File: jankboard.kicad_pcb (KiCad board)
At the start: 2 copper layers, 152.4 x 85.7 mm, 154 parts, among them J1 F31L-1A7H1-11030, J2 F31L-1A7H1-11030, J3 Conn_01x02, J4 Conn_01x02, SW1 SW_Push_45deg, SW10 SW_Push_45deg, SW11 SW_Push_45deg, SW12 SW_Push_45deg, SW13 SW_Push_45deg, SW14 SW_Push_45deg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

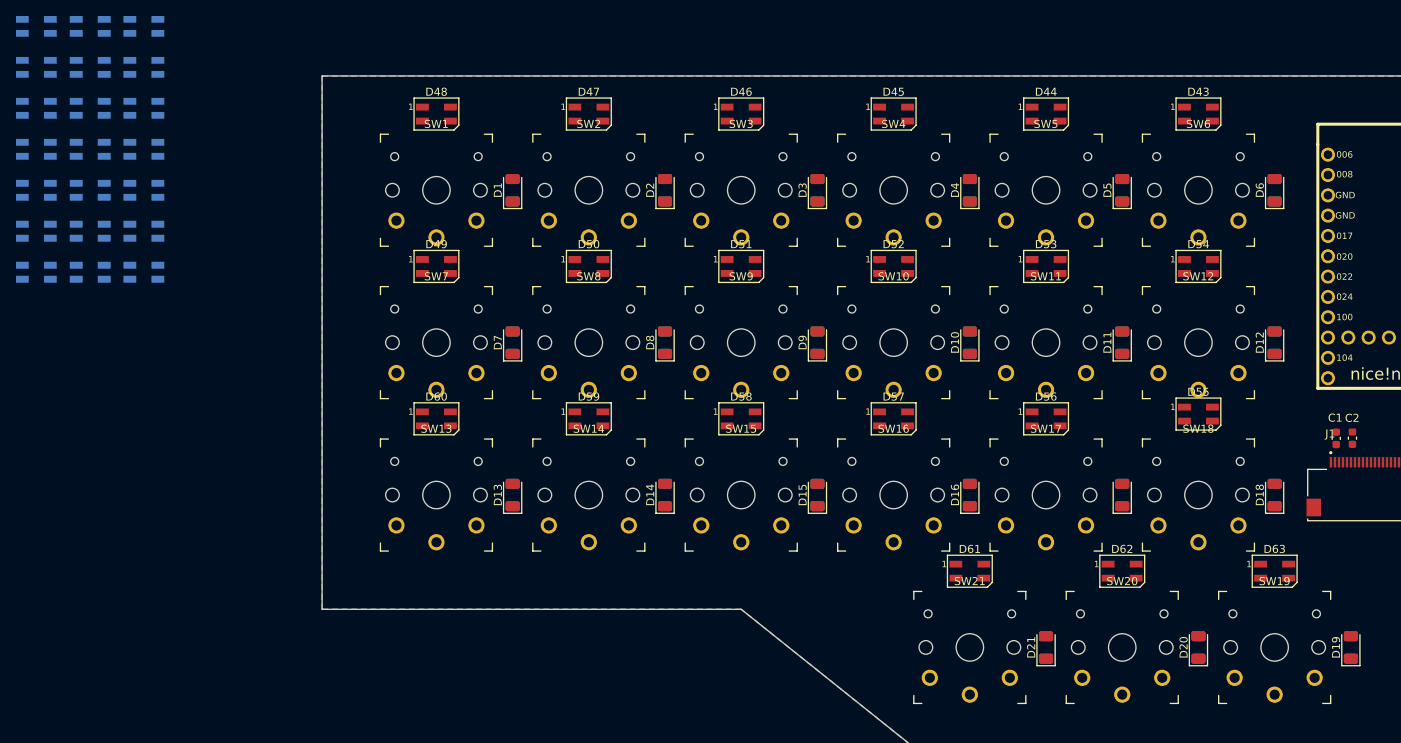
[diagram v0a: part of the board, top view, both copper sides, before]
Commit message: wired up matrix
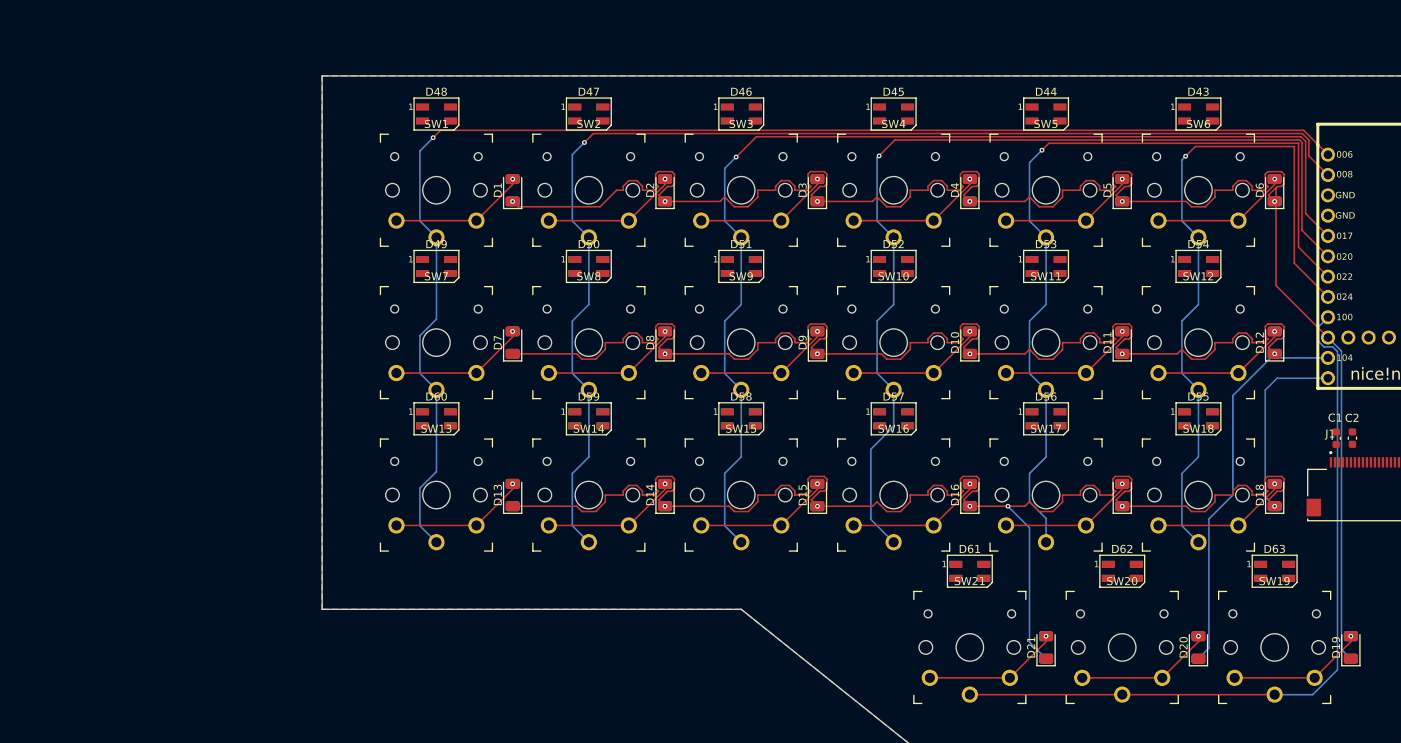
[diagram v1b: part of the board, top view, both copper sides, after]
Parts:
- moved D84 159.2 mm to (142.9, 85.7)
- moved D83 142.2 mm to (123.8, 85.7)
- moved D76 140.5 mm to (133.3, 66.7), turned to 0 degrees
- moved D75 138.9 mm to (133.3, 47.6)
- moved D64 132.3 mm to (133.3, 28.6), turned to 0 degrees
- moved D82 126.0 mm to (104.8, 85.7)
- moved D77 120.9 mm to (114.3, 66.7), turned to 0 degrees
- moved D74 120.4 mm to (114.3, 47.6)
- moved D78 117.9 mm to (95.2, 66.7), turned to 0 degrees
- moved D65 112.9 mm to (114.3, 28.6), turned to 0 degrees
- moved D73 102.4 mm to (95.2, 47.6)
- moved D79 98.5 mm to (76.2, 66.7), turned to 0 degrees
- moved D66 93.7 mm to (95.2, 28.6), turned to 0 degrees
- moved D72 85.1 mm to (76.2, 47.6)
- moved D80 79.2 mm to (57.1, 66.7), turned to 0 degrees
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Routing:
- net ROW0: track 0.00 -> 218.1 mm, vias 0 -> 6
- net ROW1: track 0.00 -> 204.2 mm, vias 0 -> 5
- net ROW2: track 0.00 -> 199.8 mm, vias 0 -> 6
- net COL0: track 0.00 -> 169.0 mm, vias 0 -> 1
- net COL1: track 0.00 -> 151.6 mm, vias 0 -> 1
- net COL2: track 0.00 -> 138.5 mm, vias 0 -> 1
- net COL3: track 0.00 -> 122.7 mm, vias 0 -> 1
- net COL4: track 0.00 -> 104.5 mm, vias 0 -> 1
- net COL6: track 0.00 -> 93.4 mm
- net COL5: track 0.00 -> 87.4 mm, vias 0 -> 1
- net Net-(D19-A): track 0.00 -> 17.1 mm, vias 0 -> 1
- net Net-(D18-A): track 0.00 -> 17.1 mm, vias 0 -> 1
- net Net-(D17-A): track 0.00 -> 17.1 mm, vias 0 -> 1
- net Net-(D16-A): track 0.00 -> 17.1 mm, vias 0 -> 1
- net Net-(D12-A): track 0.00 -> 17.1 mm, vias 0 -> 1
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
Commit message: neopixels
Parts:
- turned D49 to 180 degrees
- turned D50 to 180 degrees
- turned D51 to 180 degrees
- turned D52 to 180 degrees
- turned D53 to 180 degrees
- turned D54 to 180 degrees
- turned D61 to 180 degrees
- turned D62 to 180 degrees
- turned D63 to 180 degrees
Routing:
- net +3.3V: track 0.00 -> 535.6 mm, vias 0 -> 22
- net Net-(D60-DOUT): track 0.00 -> 90.0 mm
- net Net-(D81-DOUT): track 0.00 -> 85.3 mm, vias 0 -> 2
- net Net-(D75-DOUT): track 0.00 -> 24.1 mm, vias 0 -> 1
- net Net-(D48-DOUT): track 0.00 -> 22.1 mm, vias 0 -> 3
- net Net-(D54-DOUT): track 0.00 -> 21.3 mm, vias 0 -> 2
- net Net-(D69-DOUT): track 0.00 -> 20.2 mm
- net Net-(D82-DOUT): track 0.00 -> 16.3 mm, vias 0 -> 2
- net Net-(D83-DOUT): track 0.00 -> 16.3 mm, vias 0 -> 2
- net Net-(D79-DOUT): track 0.00 -> 16.3 mm
- net Net-(D71-DOUT): track 0.00 -> 16.3 mm
- net Net-(D67-DOUT): track 0.00 -> 16.3 mm
- net Net-(D58-DOUT): track 0.00 -> 16.3 mm
- net Net-(D50-DOUT): track 0.00 -> 16.3 mm
- net Net-(D46-DOUT): track 0.00 -> 16.3 mm
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
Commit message: connectors
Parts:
- J3, J4: footprint Connector_JST:JST_EH_S2B-EH_1x02_P2.50mm_Horizontal -> Connector_JST:JST_PH_S2B-PH-SM4-TB_1x02-1MP_P2.00mm_Horizontal
- R1, R2, R5, R6: footprint Resistor_SMD:R_0612_1632Metric -> Resistor_SMD:R_0603_1608Metric
- R3, R4, R7, R8: footprint Resistor_SMD:R_0612_1632Metric -> Resistor_SMD:R_0603_1608Metric; moved to B.Cu
- moved C18 211.6 mm to (145.0, 77.0), turned to -90 degrees
- moved C19 202.2 mm to (146.5, 77.0), turned to -90 degrees
- moved C20 197.8 mm to (151.0, 77.0), turned to 90 degrees
- moved C21 196.5 mm to (152.5, 77.0), turned to 90 degrees
- moved C22 195.2 mm to (154.0, 77.0), turned to 90 degrees
- moved C23 194.0 mm to (155.5, 77.0), turned to 90 degrees
- moved C24 192.8 mm to (157.0, 77.0), turned to 90 degrees
- moved C26 191.7 mm to (159.0, 77.0), turned to 90 degrees
- moved C27 189.5 mm to (161.5, 78.5)
- moved C25 188.8 mm to (161.5, 76.5)
- moved C28 181.5 mm to (161.5, 80.5)
- moved C31 177.4 mm to (166.0, 80.5)
- moved C30 177.3 mm to (166.0, 78.5)
- moved C29 177.2 mm to (166.0, 76.5)
- moved C34 174.6 mm to (171.0, 71.5)
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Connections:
- C18 pad 1: GND -> +3.3V
- C18 pad 2: Net-(C18-Pad2) -> GND
- C19 pad 1: GND -> +3.3V
- C19 pad 2: Net-(C18-Pad2) -> GND
- C20 pad 2: Net-(D86-A) -> Net-(C20-Pad2)
- C21 pad 1: +3.3V -> GND
- C21 pad 2: GND -> Net-(C20-Pad2)
- C25 pad 1: +3.3V -> Net-(C25-Pad1)
- C25 pad 2: GND -> Net-(C25-Pad2)
- C26 pad 2: Net-(C26-Pad2) -> Net-(D86-A)
- C27 pad 1: GND -> Net-(C27-Pad1)
- C28 pad 1: GND -> Net-(C28-Pad1)
- C32 pad 1: Net-(C32-Pad1) -> GND
- C33 pad 1: Net-(C33-Pad1) -> GND
- C34 pad 1: Net-(C34-Pad1) -> GND
- J2 pad 11: Net-(C18-Pad2) -> Net-(C20-Pad2)
- J2 pad 16: Net-(C29-Pad2) -> Net-(C25-Pad2)
- J2 pad 17: Net-(C29-Pad1) -> Net-(C25-Pad1)
- J2 pad 18: Net-(C30-Pad2) -> Net-(C27-Pad2)
- J2 pad 19: Net-(C30-Pad1) -> Net-(C27-Pad1)
- J2 pad 20: Net-(C31-Pad2) -> Net-(C28-Pad2)
- J2 pad 21: Net-(C31-Pad1) -> Net-(C28-Pad1)
- J2 pad 22: Net-(C32-Pad2) -> Net-(C29-Pad2)
- J2 pad 23: Net-(C32-Pad1) -> Net-(C29-Pad1)
- J2 pad 24: Net-(C33-Pad2) -> Net-(C30-Pad2)
- J2 pad 25: Net-(C33-Pad1) -> Net-(C30-Pad1)
- J2 pad 26: Net-(C34-Pad2) -> Net-(C31-Pad2)
- J2 pad 27: Net-(C34-Pad1) -> Net-(C31-Pad1)
- J2 pad 28: Net-(C26-Pad2) -> Net-(C32-Pad2)
- J2 pad 29: Net-(C27-Pad2) -> Net-(C33-Pad2)
- J2 pad 30: Net-(C28-Pad2) -> Net-(C34-Pad2)
- U1 pad 13: NEO -> SDA
- U1 pad 14: SDA -> SCL
- U1 pad 15: SCL -> DIN
- U1 pad 16: DIN -> SCK
- U1 pad 17: SCK -> CS
- U1 pad 18: CS -> DC
- U1 pad 19: DC -> BUSY
- U1 pad 20: BUSY -> NEO
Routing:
- net +3.3V: track 535.6 -> 610.1 mm, vias 22 -> 24
- net Net-(J3-Pin_1): track 0.00 -> 62.4 mm, vias 0 -> 1
- net NEO: track 0.00 -> 35.1 mm
- net BUSY: track 0.00 -> 31.0 mm
- net DC: track 0.00 -> 29.2 mm
- net CS: track 0.00 -> 26.4 mm
- net SCK: track 0.00 -> 22.5 mm
- net DIN: track 0.00 -> 19.8 mm
- net ROW0: track 218.1 -> 235.2 mm
- net Net-(C31-Pad2): track 0.00 -> 15.1 mm
- net Net-(C14-Pad2): track 0.00 -> 14.3 mm
- net Net-(C31-Pad1): track 0.00 -> 14.1 mm
- net Net-(C28-Pad2): track 0.00 -> 13.9 mm
- net Net-(C11-Pad2): track 0.00 -> 13.4 mm
- net Net-(C30-Pad2): track 0.00 -> 13.1 mm
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
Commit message: design rule checking
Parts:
- added J5: Conn_01x04_Pin, Connector_PinHeader_1.00mm:PinHeader_1x04_P1.00mm_Vertical, F.Cu at (170.8, 59.0)
- added S1: EGJ1210AAG2R, KiCad:EGJ1210AAG2R, F.Cu at (176.2, 46.5)
- added S2: EGJ1210AAG2R, KiCad:EGJ1210AAG2R, B.Cu at (176.2, 46.5)
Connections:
- U1 pad 24: Net-(J3-Pin_1) -> Net-(S1-NO)
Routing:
- net Net-(S1-NO): track 0.00 -> 24.0 mm, vias 0 -> 1
- net SDA: track 4.84 -> 12.6 mm
- net SCL: track 3.15 -> 10.5 mm
- net +3.3V: track 610.1 -> 617.4 mm
- net Net-(J3-Pin_1): track 62.4 -> 56.3 mm, vias 1 -> 2

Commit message: ????
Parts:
- moved J5 0.65 mm to (171.4, 59.0)
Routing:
- net GND: track 0.00 -> 75.0 mm, vias 0 -> 21
- net +3.3V: track 617.4 -> 651.5 mm, vias 24 -> 26
- net DIN: track 19.8 -> 34.6 mm, vias 0 -> 1
- net SCK: track 22.5 -> 34.8 mm, vias 0 -> 1
- net CS: track 26.4 -> 37.5 mm, vias 0 -> 1
- net DC: track 29.2 -> 38.9 mm, vias 0 -> 1
- net BUSY: track 31.0 -> 38.8 mm, vias 0 -> 1
- net NEO: track 35.1 -> 39.7 mm, vias 0 -> 1
- net Net-(D48-DOUT): track 22.1 -> 20.8 mm, vias 3 -> 2
- net SCL: track 10.5 -> 11.2 mm, vias 1 -> 2
- net SDA: track 12.6 -> 13.2 mm
- net ROW2: vias 6 -> 8
- net ROW1: vias 5 -> 7
- net ROW0: vias 6 -> 7

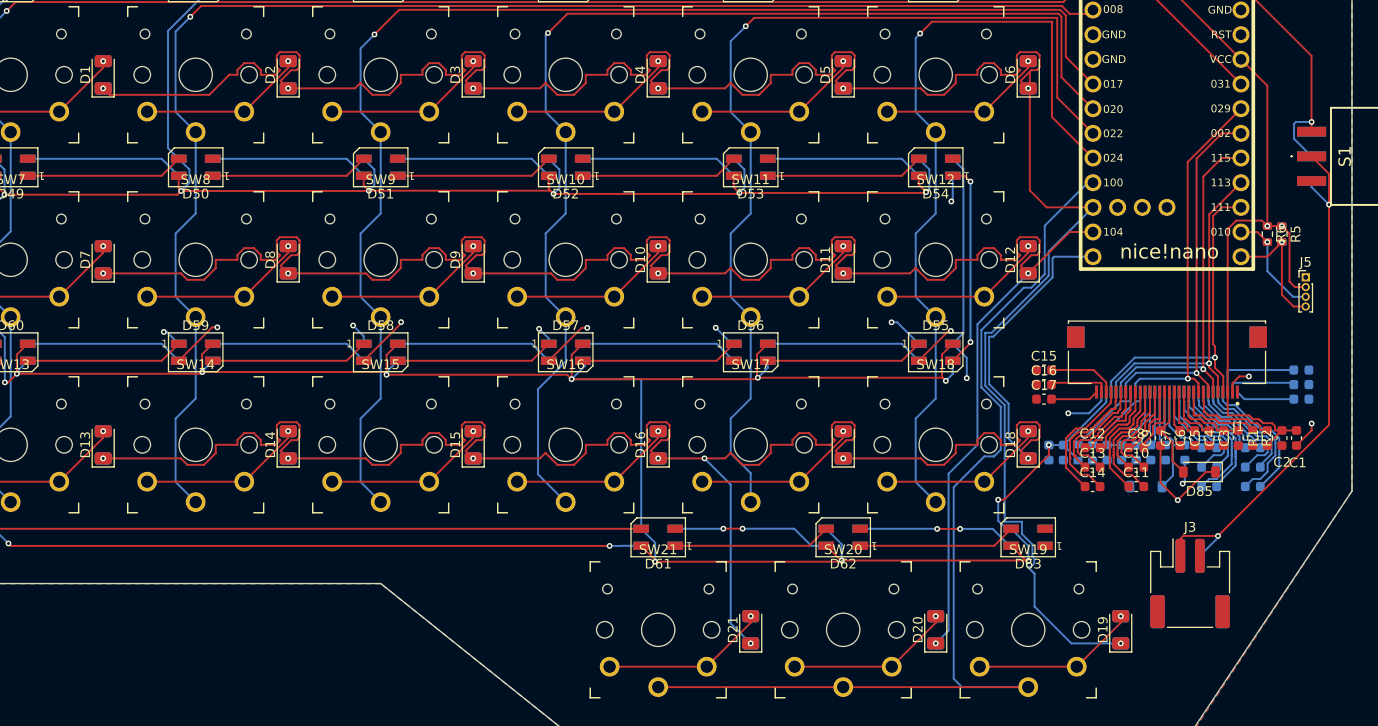
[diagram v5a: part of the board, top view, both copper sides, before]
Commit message: remove via on pins, change pin footprint
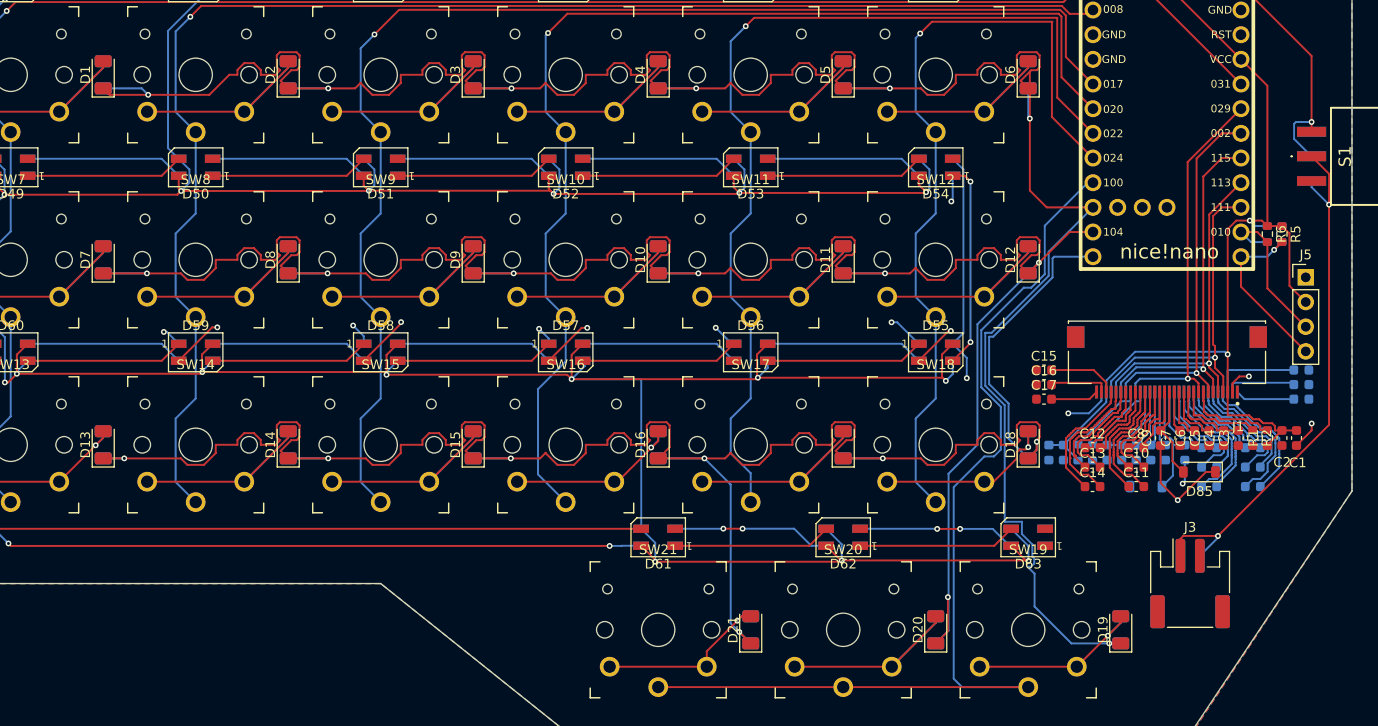
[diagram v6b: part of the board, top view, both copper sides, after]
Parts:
- J5: footprint Connector_PinHeader_1.00mm:PinHeader_1x04_P1.00mm_Vertical -> Connector_PinHeader_2.54mm:PinHeader_1x04_P2.54mm_Vertical
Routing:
- net ROW1: track 206.5 -> 234.5 mm
- net ROW0: track 235.2 -> 261.3 mm
- net ROW2: track 205.8 -> 226.6 mm, vias 8 -> 7
- net +3.3V: track 651.5 -> 659.5 mm, vias 26 -> 24
- net Net-(D20-A): track 17.1 -> 24.1 mm, vias 1 -> 0
- net Net-(D17-A): track 17.1 -> 24.1 mm, vias 1 -> 0
- net Net-(D12-A): track 17.1 -> 24.1 mm, vias 1 -> 0
- net Net-(D11-A): track 17.1 -> 24.1 mm, vias 1 -> 0
- net Net-(D10-A): track 17.1 -> 24.1 mm, vias 1 -> 0
- net Net-(D29-A): track 17.1 -> 24.1 mm, vias 1 -> 0
- net Net-(D28-A): track 17.1 -> 24.1 mm, vias 1 -> 0
- net Net-(D27-A): track 17.1 -> 24.1 mm, vias 1 -> 0
- net Net-(D26-A): track 17.1 -> 24.1 mm, vias 1 -> 0
- net Net-(D25-A): track 17.1 -> 24.1 mm, vias 1 -> 0
- net Net-(D14-A): track 17.1 -> 24.1 mm, vias 1 -> 0
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
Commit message: add led switch
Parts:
- added S3: EGJ1210AAG2R, KiCad:EGJ1210AAG2R, F.Cu at (173.6, 33.0)
- added S4: EGJ1210AAG2R, KiCad:EGJ1210AAG2R, B.Cu at (173.6, 33.0)
- moved S1 2.70 mm to (173.6, 46.6)
- moved S2 2.70 mm to (173.6, 46.6)
- moved J5 1.65 mm to (169.8, 58.9)
- moved C32 1.50 mm to (169.5, 68.5)
- moved C33 1.50 mm to (169.5, 70.0)
- moved C34 1.50 mm to (169.5, 71.5)
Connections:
- D43 pad 4: +3.3V -> NP
- D44 pad 4: +3.3V -> NP
- D45 pad 4: +3.3V -> NP
- D46 pad 4: +3.3V -> NP
- D47 pad 4: +3.3V -> NP
- D48 pad 4: +3.3V -> NP
- D49 pad 4: +3.3V -> NP
- D50 pad 4: +3.3V -> NP
- D51 pad 4: +3.3V -> NP
- D52 pad 4: +3.3V -> NP
- D53 pad 4: +3.3V -> NP
- D54 pad 4: +3.3V -> NP
- D55 pad 4: +3.3V -> NP
- D56 pad 4: +3.3V -> NP
- D57 pad 4: +3.3V -> NP
- D58 pad 4: +3.3V -> NP
- D59 pad 4: +3.3V -> NP
- D60 pad 4: +3.3V -> NP
- D61 pad 4: +3.3V -> NP
- D62 pad 4: +3.3V -> NP
- D63 pad 4: +3.3V -> NP
- D64 pad 4: +3.3V -> NP
- D65 pad 4: +3.3V -> NP
- D66 pad 4: +3.3V -> NP
- D67 pad 4: +3.3V -> NP
- D68 pad 4: +3.3V -> NP
- D69 pad 4: +3.3V -> NP
- D70 pad 4: +3.3V -> NP
- D71 pad 4: +3.3V -> NP
- D72 pad 4: +3.3V -> NP
- D73 pad 4: +3.3V -> NP
- D74 pad 4: +3.3V -> NP
- D75 pad 4: +3.3V -> NP
- D76 pad 4: +3.3V -> NP
- D77 pad 4: +3.3V -> NP
- D78 pad 4: +3.3V -> NP
- D79 pad 4: +3.3V -> NP
- D80 pad 4: +3.3V -> NP
- D81 pad 4: +3.3V -> NP
- D82 pad 4: +3.3V -> NP
- D83 pad 4: +3.3V -> NP
- D84 pad 4: +3.3V -> NP
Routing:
- net NP: track 0.00 -> 577.8 mm, vias 0 -> 23
- net +3.3V: track 659.5 -> 103.6 mm, vias 24 -> 2
- net Net-(S1-NO): track 24.0 -> 29.2 mm
- net NEO: track 39.7 -> 43.3 mm
- net Net-(J3-Pin_1): track 56.3 -> 58.8 mm
- net GND: track 75.0 -> 76.9 mm, vias 21 -> 23
- net Net-(C34-Pad2): track 6.12 -> 4.62 mm
- net Net-(C33-Pad2): track 7.26 -> 5.76 mm
- net Net-(C32-Pad2): track 9.08 -> 7.58 mm
- net SCL: track 16.6 -> 15.8 mm
- net SDA: track 18.5 -> 17.7 mm
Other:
- board size 152.4 x 85.7 mm -> 145.3 x 81 mm
